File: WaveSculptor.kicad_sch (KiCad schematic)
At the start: 0 parts

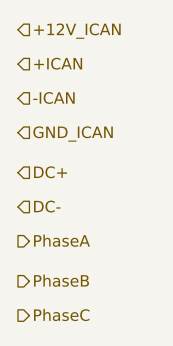
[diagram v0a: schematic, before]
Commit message: Updated Controls + Telemetry
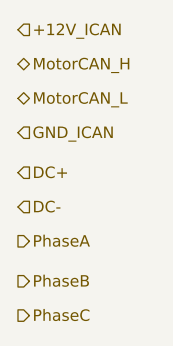
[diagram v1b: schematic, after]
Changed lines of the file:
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@@
 		)
 	)
-	(hierarchical_label "+ICAN"
-		(shape input)
+	(hierarchical_label "MotorCAN_H"
+		(shape bidirectional)
 		(at 102.87 80.645 0)
 		(effects
@@
 		)
 	)
-	(hierarchical_label "-ICAN"
-		(shape input)
+	(hierarchical_label "MotorCAN_L"
+		(shape bidirectional)
 		(at 102.87 84.455 0)
 		(effects
